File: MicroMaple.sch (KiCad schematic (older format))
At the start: 1 part

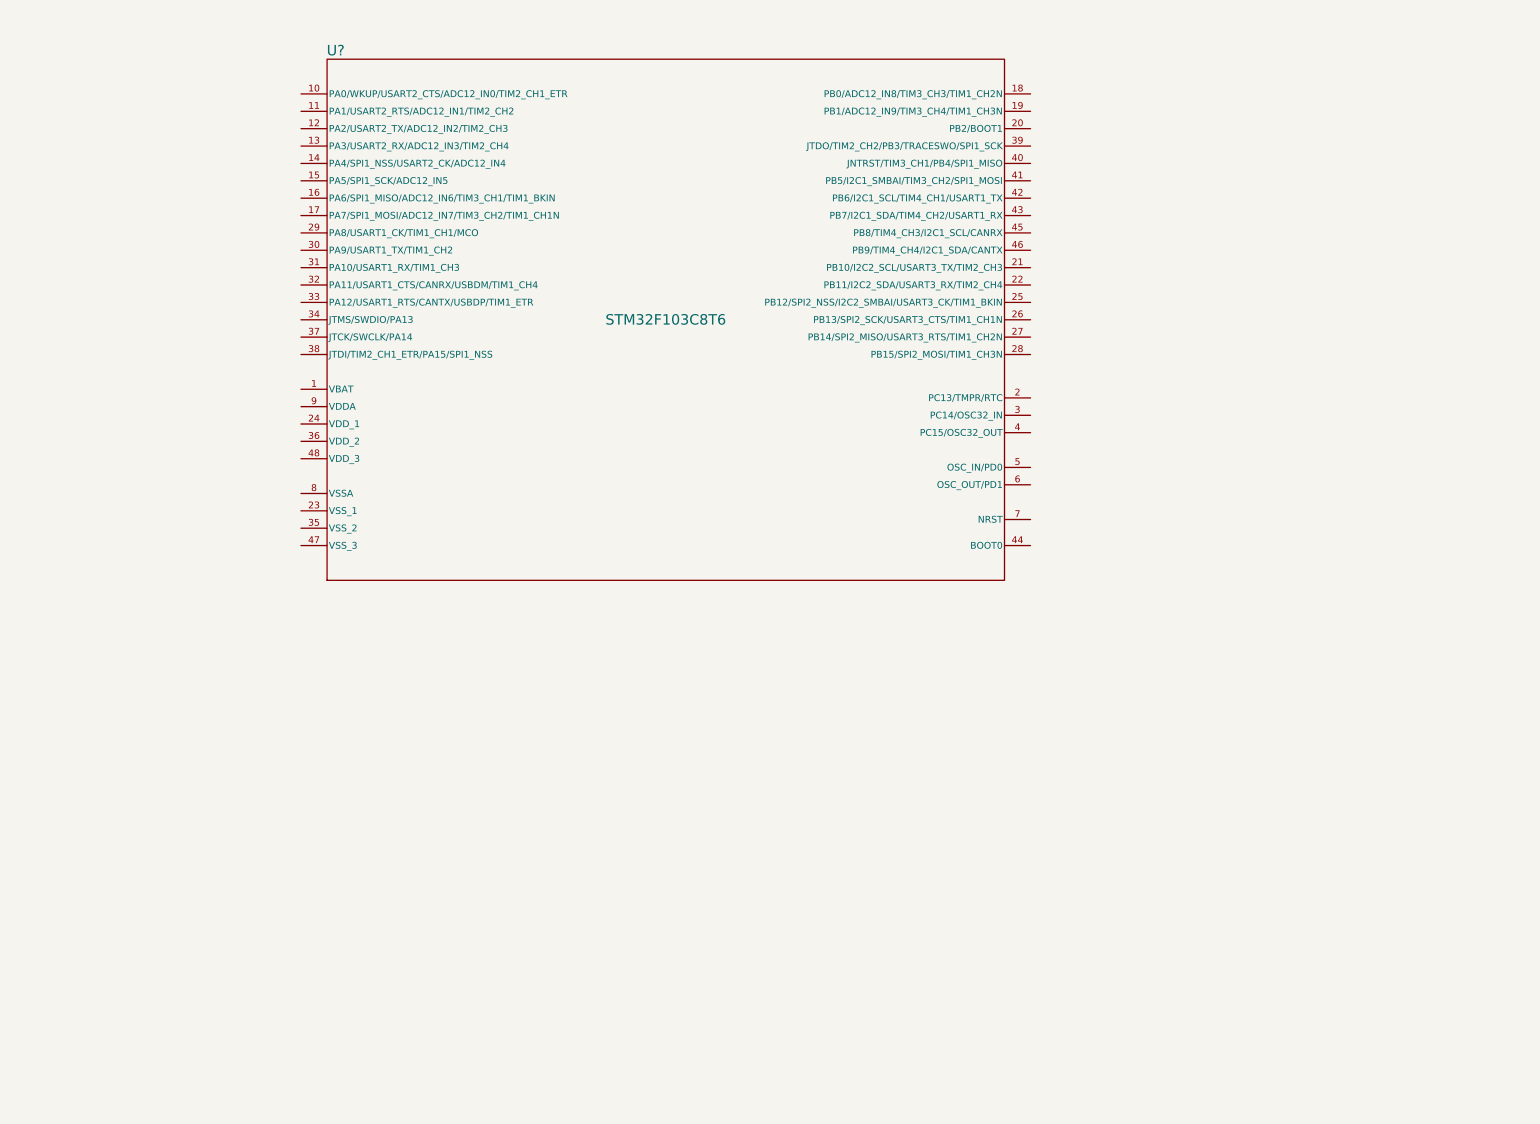
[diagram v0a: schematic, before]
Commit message: finish the sch, and assign some footprints, update the README.md
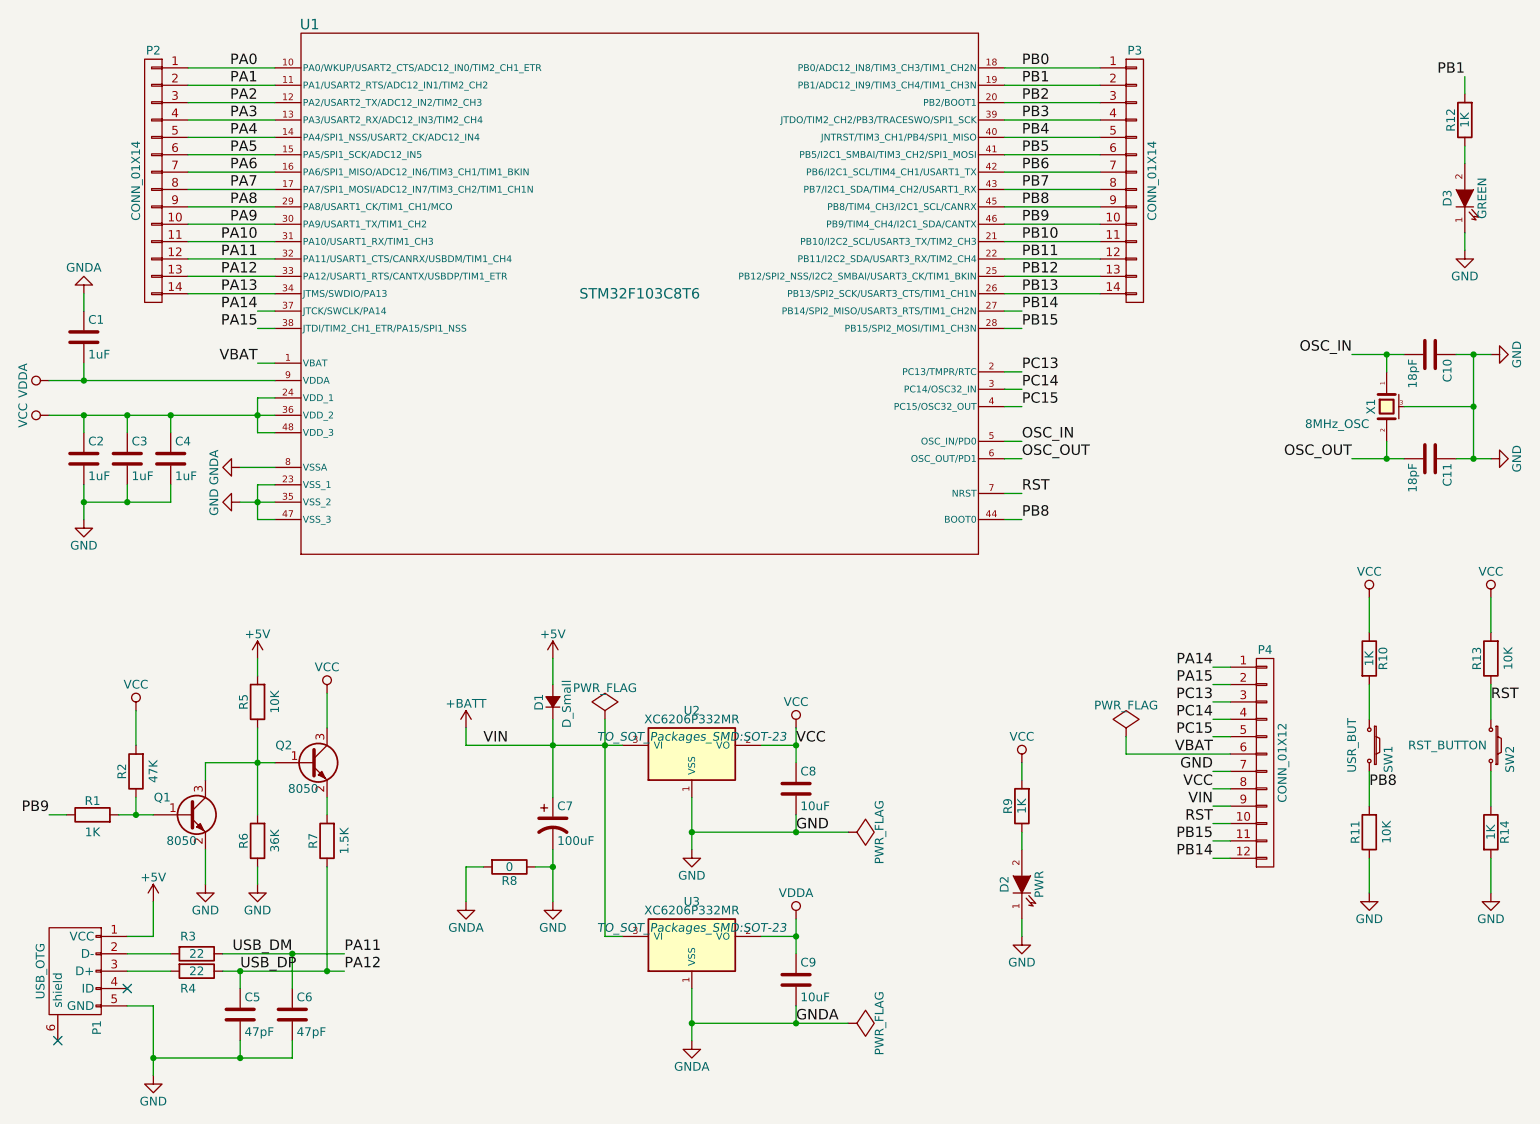
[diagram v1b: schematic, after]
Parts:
- added C1, C2, C3, C4: 1uF, Capacitors_SMD:C_0603, symbol C
- added C10, C11: 18pF, Capacitors_SMD:C_0603, symbol C
- added C5, C6: 47pF, Capacitors_SMD:C_0603, symbol C
- added C7: 100uF, SMD_Packages:SMD-1210_Pol, symbol CP1
- added C8, C9: 10uF, Capacitors_SMD:C_0603, symbol C
- added D1: D_Small, Diodes_SMD:SOD-123, symbol D_Small
- added D2: PWR, LEDs:LED_0603, symbol LED
- added D3: GREEN, LEDs:LED_0603, symbol LED
- added P1: USB_OTG, symbol USB_OTG
- added P2, P3: CONN_01X14, symbol CONN_01X14
- added P4: CONN_01X12, symbol CONN_01X12
- added Q1, Q2: 8050, TO_SOT_Packages_SMD:SOT-23, symbol Q_NPN_BEC
- added R1, R10, R12, R14, R9: 1K, Resistors_SMD:R_0603, symbol R
- added R11, R13, R5: 10K, Resistors_SMD:R_0603, symbol R
- added R2: 47K, Resistors_SMD:R_0603, symbol R
- added R3, R4: 22, Resistors_SMD:R_0603, symbol R
- added R6: 36K, Resistors_SMD:R_0603, symbol R
- added R7: 1.5K, Resistors_SMD:R_0603, symbol R
- added R8: 0, Resistors_SMD:R_0603, symbol R
- added SW1: USR_BUT, symbol SW_PUSH_SMALL_H
- added SW2: RST_BUTTON, symbol SW_PUSH_SMALL_H
- added U2, U3: XC6206P332MR, TO_SOT_Packages_SMD:SOT-23, symbol XC6206P332MR
- added X1: 8MHz_OSC, Crystals:Resonator_7.2x3mm, symbol CRYSTAL_SMD
- gave numbers to parts that had none: 1
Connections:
- net VBAT: now reaches U1.1 (VBAT)
- net VBAT: now also P4.6 (P6)
- net PA0: now reaches U1.10 (PA0/WKUP/USART2_CTS/ADC12_IN0/TIM2_CH1_ETR)
- net PA0: now also P2.1 (P1)
- net PA1: now reaches U1.11 (PA1/USART2_RTS/ADC12_IN1/TIM2_CH2)
- net PA1: now also P2.2 (P2)
- net PA2: now reaches U1.12 (PA2/USART2_TX/ADC12_IN2/TIM2_CH3)
- net PA2: now also P2.3 (P3)
- net PA3: now reaches U1.13 (PA3/USART2_RX/ADC12_IN3/TIM2_CH4)
- net PA3: now also P2.4 (P4)
- net PA4: now reaches U1.14 (PA4/SPI1_NSS/USART2_CK/ADC12_IN4)
- net PA4: now also P2.5 (P5)
- net PA5: now reaches U1.15 (PA5/SPI1_SCK/ADC12_IN5)
- net PA5: now also P2.6 (P6)
- net PA6: now reaches U1.16 (PA6/SPI1_MISO/ADC12_IN6/TIM3_CH1/TIM1_BKIN)
- net PA6: now also P2.7 (P7)
- net PA7: now reaches U1.17 (PA7/SPI1_MOSI/ADC12_IN7/TIM3_CH2/TIM1_CH1N)
- net PA7: now also P2.8 (P8)
- net PB0: now reaches U1.18 (PB0/ADC12_IN8/TIM3_CH3/TIM1_CH2N)
- net PB0: now also P3.1 (P1)
- net PB1: now reaches U1.19 (PB1/ADC12_IN9/TIM3_CH4/TIM1_CH3N)
- net PB1: now also P3.2 (P2), R12.2
- net PC13: now reaches U1.2 (PC13/TMPR/RTC)
- net PC13: now also P4.3 (P3)
- net PB2: now reaches U1.20 (PB2/BOOT1)
- net PB2: now also P3.3 (P3)
- net PB10: now reaches U1.21 (PB10/I2C2_SCL/USART3_TX/TIM2_CH3)
- net PB10: now also P3.11 (P11)
- net PB11: now reaches U1.22 (PB11/I2C2_SDA/USART3_RX/TIM2_CH4)
- net PB11: now also P3.12 (P12)
- net GND: now reaches U1.23 (VSS_1)
- net GND: now also U1.35 (VSS_2), U1.47 (VSS_3), C10.1, C11.1, C2.2, C3.2, C4.2, C5.2, C6.2, C7.2, C8.2, D2.1 (K), D3.1 (K), P1.5 (GND), P4.7 (P7), Q1.2 (E), R11.1, R14.2, R6.1, R8.1, U2.1 (VSS), X1.3 (case)
- net VCC: now reaches U1.24 (VDD_1)
- net VCC: now also U1.36 (VDD_2), U1.48 (VDD_3), C2.1, C3.1, C4.1, C8.1, P4.8 (P8), Q2.3 (C), R10.1, R13.2, R2.2, R9.2, U2.2 (VO)
- net PB12: now reaches U1.25 (PB12/SPI2_NSS/I2C2_SMBAI/USART3_CK/TIM1_BKIN)
- net PB12: now also P3.13 (P13)
- net PB13: now reaches U1.26 (PB13/SPI2_SCK/USART3_CTS/TIM1_CH1N)
- net PB13: now also P3.14 (P14)
- net PB14: now reaches U1.27 (PB14/SPI2_MISO/USART3_RTS/TIM1_CH2N)
- net PB14: now also P4.12 (P12)
- net PB15: now reaches U1.28 (PB15/SPI2_MOSI/TIM1_CH3N)
- net PB15: now also P4.11 (P11)
- net PA8: now reaches U1.29 (PA8/USART1_CK/TIM1_CH1/MCO)
- net PA8: now also P2.9 (P9)
- net PC14: now reaches U1.3 (PC14/OSC32_IN)
- net PC14: now also P4.4 (P4)
- net PA9: now reaches U1.30 (PA9/USART1_TX/TIM1_CH2)
- net PA9: now also P2.10 (P10)
- net PA10: now reaches U1.31 (PA10/USART1_RX/TIM1_CH3)
- net PA10: now also P2.11 (P11)
- net PA11: now reaches U1.32 (PA11/USART1_CTS/CANRX/USBDM/TIM1_CH4)
- net PA11: now also C6.1, P2.12 (P12), R3.1
- net PA12: now reaches U1.33 (PA12/USART1_RTS/CANTX/USBDP/TIM1_ETR)
- net PA12: now also C5.1, P2.13 (P13), R4.1, R7.1
- net PA13: now reaches U1.34 (JTMS/SWDIO/PA13)
- net PA13: now also P2.14 (P14)
- net PA14: now reaches U1.37 (JTCK/SWCLK/PA14)
- net PA14: now also P4.1 (P1)
- net PA15: now reaches U1.38 (JTDI/TIM2_CH1_ETR/PA15/SPI1_NSS)
- net PA15: now also P4.2 (P2)
- net PB3: now reaches U1.39 (JTDO/TIM2_CH2/PB3/TRACESWO/SPI1_SCK)
- net PB3: now also P3.4 (P4)
- net PC15: now reaches U1.4 (PC15/OSC32_OUT)
- net PC15: now also P4.5 (P5)
- net PB4: now reaches U1.40 (JNTRST/TIM3_CH1/PB4/SPI1_MISO)
- net PB4: now also P3.5 (P5)
- net PB5: now reaches U1.41 (PB5/I2C1_SMBAI/TIM3_CH2/SPI1_MOSI)
- net PB5: now also P3.6 (P6)
- net PB6: now reaches U1.42 (PB6/I2C1_SCL/TIM4_CH1/USART1_TX)
- net PB6: now also P3.7 (P7)
- net PB7: now reaches U1.43 (PB7/I2C1_SDA/TIM4_CH2/USART1_RX)
- net PB7: now also P3.8 (P8)
- net PB8: now reaches U1.44 (BOOT0)
- net PB8: now also U1.45 (PB8/TIM4_CH3/I2C1_SCL/CANRX), P3.9 (P9), R11.2, SW1.2
- net PB9: now reaches U1.46 (PB9/TIM4_CH4/I2C1_SDA/CANTX)
- net PB9: now also P3.10 (P10), R1.1
- net OSC_IN: now reaches U1.5 (OSC_IN/PD0)
- net OSC_IN: now also C10.2, X1.1
- net OSC_OUT: now reaches U1.6 (OSC_OUT/PD1)
- net OSC_OUT: now also C11.2, X1.2
- net RST: now reaches U1.7 (NRST)
- net RST: now also P4.10 (P10), R13.1, SW2.1
- net GNDA: now reaches U1.8 (VSSA)
- net GNDA: now also C1.1, C9.2, R8.2, U3.1 (VSS)
- net VDDA: now reaches U1.9 (VDDA)
- net VDDA: now also C1.2, C9.1, U3.2 (VO)
- new net: P1.2 (D-), R3.2
- new net: P1.3 (D+), R4.2
- new net: D3.2 (A), R12.1
- new net: D2.2 (A), R9.1
- new net: R10.2, SW1.1
- new net: R14.1, SW2.2
- new net: Q2.2 (E), R7.2
- new net: Q1.3 (C), Q2.1 (B), R5.1, R6.2
- new net: Q1.1 (B), R1.2, R2.1
- new net +5V: D1.2 (A), P1.1 (VCC), R5.2
- new net +BATT: C7.1, D1.1 (K), P4.9 (P9), U2.3 (VI), U3.3 (VI)
- no-connect marks 0 -> 2
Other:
- moved on the sheet: U1

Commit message: finish assign the footprints and begin the PCB design
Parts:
- P1: footprint (none) -> myFootprints:USB_Micro-B-MK5
- P2, P3: footprint (none) -> myFootprints:Connector_FAD_14x1
- P4: footprint (none) -> myFootprints:Connector_FAD_12x1
- SW1, SW2: footprint (none) -> Buttons_Switches_SMD:SW_SPST_EVQP7C
- U1: footprint (none) -> Housings_QFP:LQFP-48_7x7mm_Pitch0.5mm
- X1: footprint Crystals:Resonator_7.2x3mm -> myFootprints:Resonator_3.2x1.5mm
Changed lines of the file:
@@
 F 0 "U1" H 3300 3900 60  0000 C CNN
 F 1 "STM32F103C8T6" H 5200 2350 60  0000 C CNN
-F 2 "" H 5200 2050 60  0001 C CNN
+F 2 "Housings_QFP:LQFP-48_7x7mm_Pitch0.5mm" H 5200 2050 60  0001 C CNN
 F 3 "" H 5200 2050 60  0000 C CNN
 	1    5200 2350
@@
 F 0 "P1" H 2275 6125 50  0000 C CNN
 F 1 "USB_OTG" H 1950 6450 50  0000 C CNN
-F 2 "" V 1900 6150 50  0001 C CNN
+F 2 "myFootprints:USB_Micro-B-MK5" V 1900 6150 50  0001 C CNN
 F 3 "" V 1900 6150 50  0000 C CNN
 	1    1950 6250
@@
 F 0 "P2" H 2400 2450 50  0000 C CNN
 F 1 "CONN_01X14" V 2500 1700 50  0000 C CNN
-F 2 "" H 2400 1700 50  0001 C CNN
+F 2 "myFootprints:Connector_FAD_14x1" H 2400 1700 50  0001 C CNN
 F 3 "" H 2400 1700 50  0000 C CNN
 	1    2400 1700
@@
 F 0 "P3" H 8050 2450 50  0000 C CNN
 F 1 "CONN_01X14" V 8150 1700 50  0000 C CNN
-F 2 "" H 8050 1700 50  0001 C CNN
+F 2 "myFootprints:Connector_FAD_14x1" H 8050 1700 50  0001 C CNN
 F 3 "" H 8050 1700 50  0000 C CNN
 	1    8050 1700
@@
 F 0 "X1" H 9500 3090 50  0000 C CNN
 F 1 "8MHz_OSC" V 9600 3100 50  0000 L CNN
-F 2 "Crystals:Resonator_7.2x3mm" H 9500 3000 50  0001 C CNN
+F 2 "myFootprints:Resonator_3.2x1.5mm" H 9500 3000 50  0001 C CNN
 F 3 "" H 9500 3000 50  0000 C CNN
 	1    9500 3000
@@
 F 0 "SW1" H 9480 5060 50  0000 C CNN
 F 1 "USR_BUT" H 9400 4850 50  0000 C CNN
-F 2 "" H 9400 5150 50  0001 C CNN
+F 2 "Buttons_Switches_SMD:SW_SPST_EVQP7C" H 9400 5150 50  0001 C CNN
 F 3 "" H 9400 5150 50  0000 C CNN
 	1    9400 4950
@@
 F 0 "SW2" H 10180 5060 50  0000 C CNN
 F 1 "RST_BUTTON" V 10100 4700 50  0000 C CNN
-F 2 "" H 10100 5150 50  0001 C CNN
+F 2 "Buttons_Switches_SMD:SW_SPST_EVQP7C" H 10100 5150 50  0001 C CNN
 F 3 "" H 10100 5150 50  0000 C CNN
 	1    10100 4950
@@
 F 0 "P4" H 8800 5700 50  0000 C CNN
 F 1 "CONN_01X12" V 8900 5050 50  0000 C CNN
-F 2 "" H 8800 5050 50  0001 C CNN
+F 2 "myFootprints:Connector_FAD_12x1" H 8800 5050 50  0001 C CNN
 F 3 "" H 8800 5050 50  0000 C CNN
 	1    8800 5050

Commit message: finish the PCB design
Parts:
- added P5, P6, P7, P8: CONN_01X01, myFootprints:Debug_Pin_1, symbol CONN_01X01
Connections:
- net GND: now also P8.1 (P1)
- net PA13: now also P5.1 (P1)
- net PA14: now also P6.1 (P1)
- net VCC: now also P7.1 (P1)
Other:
- note added: "Debug_Port"
- note added: "SWCLK"
- note added: "SWDIO"
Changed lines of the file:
@@
 	0    -1   -1   0
 $EndComp
+$Comp
+L CONN_01X01 P5
+U 1 1 57FB1749
+P 9450 1200
+F 0 "P5" H 9450 1300 50  0000 C CNN
+F 1 "CONN_01X01" H 9250 1100 50  0000 C CNN
+F 2 "myFootprints:Debug_Pin_1" H 9450 1200 50  0001 C CNN
+F 3 "" H 9450 1200 50  0000 C CNN
+	1    9450 1200
+	1    0    0    1
+$EndComp
+$Comp
+L CONN_01X01 P6
+U 1 1 57FB1A6E
+P 9450 1500
+F 0 "P6" H 9450 1600 50  0000 C CNN
+F 1 "CONN_01X01" H 9250 1400 50  0000 C CNN
+F 2 "myFootprints:Debug_Pin_1" H 9450 1500 50  0001 C CNN
+F 3 "" H 9450 1500 50  0000 C CNN
+	1    9450 1500
+	1    0    0    1
+$EndComp
+$Comp
+L CONN_01X01 P7
+U 1 1 57FB1E48
+P 9450 1800
+F 0 "P7" H 9450 1900 50  0000 C CNN
+F 1 "CONN_01X01" H 9250 1700 50  0000 C CNN
+F 2 "myFootprints:Debug_Pin_1" H 9450 1800 50  0001 C CNN
+F 3 "" H 9450 1800 50  0000 C CNN
+	1    9450 1800
+	1    0    0    1
+$EndComp
+$Comp
+L CONN_01X01 P8
+U 1 1 57FB1EE3
+P 9450 2100
+F 0 "P8" H 9450 2200 50  0000 C CNN
+F 1 "CONN_01X01" H 9250 2000 50  0000 C CNN
+F 2 "myFootprints:Debug_Pin_1" H 9450 2100 50  0001 C CNN
+F 3 "" H 9450 2100 50  0000 C CNN
+	1    9450 2100
+	1    0    0    1
+$EndComp
+Wire Wire Line
+	9250 1200 9150 1200
+Wire Wire Line
+	9250 1500 9150 1500
+Wire Wire Line
+	9250 1800 9150 1800
+Wire Wire Line
+	9250 2100 9150 2100
+Text Label 9150 1200 2    60   ~ 0
+PA13
+Text Label 9150 1500 2    60   ~ 0
+PA14
+Text Label 9150 1800 2    60   ~ 0
+VCC
+Text Label 9150 2100 2    60   ~ 0
+GND
+Text Notes 8650 1000 0    100  ~ 0
+Debug_Port
+Text Notes 8550 1200 0    60   ~ 0
+SWDIO
+Text Notes 8550 1500 0    60   ~ 0
+SWCLK
 $EndSCHEMATC
